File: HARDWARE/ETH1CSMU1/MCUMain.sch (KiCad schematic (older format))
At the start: 31 parts, among them J701 Conn_02x05, U701 STM32F746ZETx, U702 24LC08, X701 CRYSTAL_4PIN

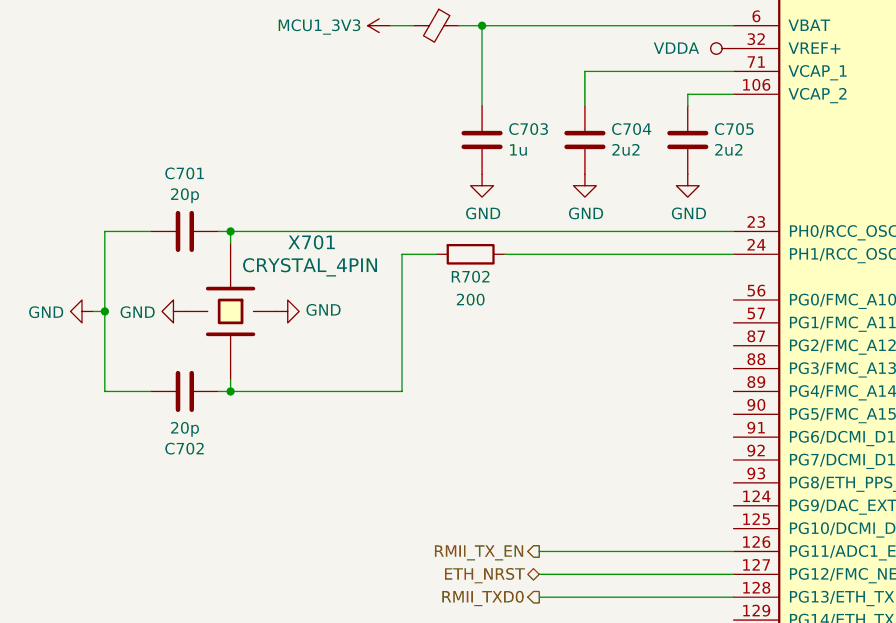
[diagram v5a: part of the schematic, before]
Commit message: Redesigned feedback circuit.
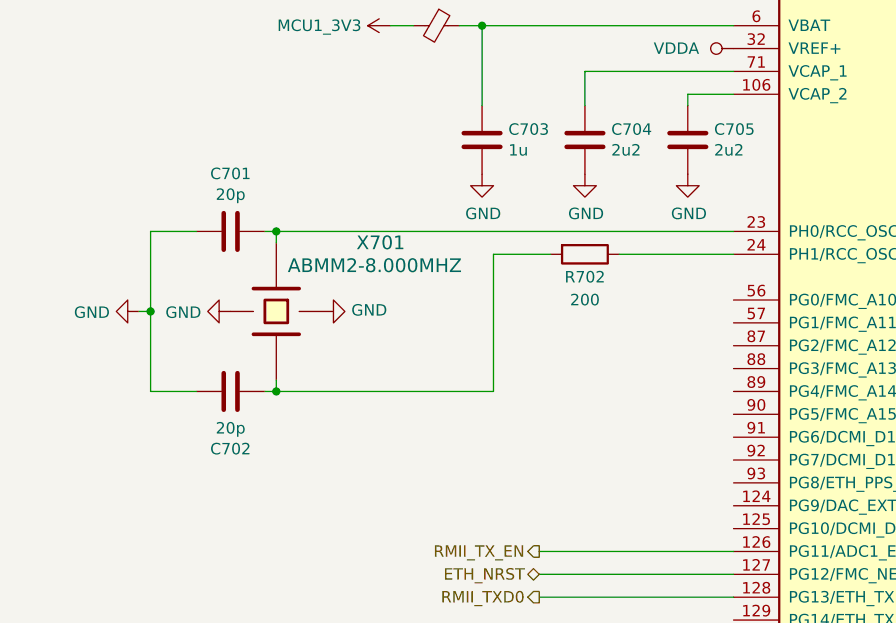
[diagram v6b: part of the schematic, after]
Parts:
- R702: footprint (none) -> Resistors_SMD:R_0603
- X701: value CRYSTAL_4PIN -> ABMM2-8.000MHZ
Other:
- moved on the sheet: C701, C702, R702, X701
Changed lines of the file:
@@
 L crystal_local:CRYSTAL_4PIN X?
 U 1 1 5BE349FE
-P 1450 3950
+P 1650 3950
 AR Path="/5BE0F4FE/5BE349FE" Ref="X?"  Part="1"
 AR Path="/5BE4235D/5BE349FE" Ref="X701"  Part="1"
-F 0 "X701" V 1150 4200 60  0000 L CNN
-F 1 "CRYSTAL_4PIN" V 1250 4000 60  0000 L CNN
-F 2 "" H 1450 3950 60  0001 C CNN
-F 3 "" H 1450 3950 60  0000 C CNN
+F 0 "X701" V 1350 4300 60  0000 L CNN
+F 1 "ABMM2-8.000MHZ" V 1450 4000 60  0000 L CNN
+F 2 "" H 1650 3950 60  0001 C CNN
+F 3 "" H 1650 3950 60  0000 C CNN
+	1    1650 3950
+	0    1    1    0
+$EndComp
+Wire Wire Line
+	1650 3650 1650 3600
+Wire Wire Line
+	1650 4250 1650 4300
+Wire Wire Line
+	1650 4300 2600 4300
+$Comp
+L Device:C C?
+U 1 1 5BE34A08
+P 1450 3600
+AR Path="/5BE0F4FE/5BE34A08" Ref="C?"  Part="1"
+AR Path="/5BE4235D/5BE34A08" Ref="C701"  Part="1"
+F 0 "C701" V 1198 3600 50  0000 C CNN
+F 1 "20p" V 1289 3600 50  0000 C CNN
+F 2 "Capacitors_SMD:C_0603" H 1488 3450 50  0001 C CNN
+F 3 "~" H 1450 3600 50  0001 C CNN
+	1    1450 3600
+	0    1    1    0
+$EndComp
+Wire Wire Line
+	1600 3600 1650 3600
+$Comp
+L Device:C C?
+U 1 1 5BE34A11
+P 1450 4300
+AR Path="/5BE0F4FE/5BE34A11" Ref="C?"  Part="1"
+AR Path="/5BE4235D/5BE34A11" Ref="C702"  Part="1"
+F 0 "C702" V 1702 4300 50  0000 C CNN
+F 1 "20p" V 1611 4300 50  0000 C CNN
+F 2 "Capacitors_SMD:C_0603" H 1488 4150 50  0001 C CNN
+F 3 "~" H 1450 4300 50  0001 C CNN
+	1    1450 4300
+	0    -1   1    0
+$EndComp
+Wire Wire Line
+	1600 4300 1650 4300
+Connection ~ 1650 4300
+Wire Wire Line
+	1300 4300 1100 4300
+Wire Wire Line
+	1100 4300 1100 3950
+Wire Wire Line
+	1100 3600 1300 3600
+Wire Wire Line
+	1050 3950 1100 3950
+Connection ~ 1100 3950
+Wire Wire Line
+	1100 3950 1100 3600
+$Comp
+L power:GND #PWR?
+U 1 1 5BE34A20
+P 1450 3950
+AR Path="/5BE0F4FE/5BE34A20" Ref="#PWR?"  Part="1"
+AR Path="/5BE4235D/5BE34A20" Ref="#PWR0101"  Part="1"
+F 0 "#PWR0101" H 1450 3700 50  0001 C CNN
+F 1 "GND" V 1455 3822 50  0000 R CNN
+F 2 "" H 1450 3950 50  0001 C CNN
+F 3 "" H 1450 3950 50  0001 C CNN
 	1    1450 3950
 	0    1    1    0
 $EndComp
-Wire Wire Line
-	1450 3650 1450 3600
-Wire Wire Line
-	1450 4250 1450 4300
-Wire Wire Line
-	1450 4300 2200 4300
-$Comp
-L Device:C C?
-U 1 1 5BE34A08
-P 1250 3600
-AR Path="/5BE0F4FE/5BE34A08" Ref="C?"  Part="1"
-AR Path="/5BE4235D/5BE34A08" Ref="C701"  Part="1"
-F 0 "C701" V 998 3600 50  0000 C CNN
-F 1 "20p" V 1089 3600 50  0000 C CNN
-F 2 "Capacitors_SMD:C_0603" H 1288 3450 50  0001 C CNN
-F 3 "~" H 1250 3600 50  0001 C CNN
-	1    1250 3600
-	0    1    1    0
-$EndComp
-Wire Wire Line
-	1400 3600 1450 3600
-Connection ~ 1450 3600
-$Comp
-L Device:C C?
-U 1 1 5BE34A11
-P 1250 4300
-AR Path="/5BE0F4FE/5BE34A11" Ref="C?"  Part="1"
-AR Path="/5BE4235D/5BE34A11" Ref="C702"  Part="1"
-F 0 "C702" V 1502 4300 50  0000 C CNN
-F 1 "20p" V 1411 4300 50  0000 C CNN
-F 2 "Capacitors_SMD:C_0603" H 1288 4150 50  0001 C CNN
-F 3 "~" H 1250 4300 50  0001 C CNN
-	1    1250 4300
-	0    -1   1    0
-$EndComp
-Wire Wire Line
-	1400 4300 1450 4300
-Connection ~ 1450 4300
-Wire Wire Line
-	1100 4300 900  4300
-Wire Wire Line
-	900  4300 900  3950
-Wire Wire Line
-	900  3600 1100 3600
-Wire Wire Line
-	850  3950 900  3950
-Connection ~ 900  3950
-Wire Wire Line
-	900  3950 900  3600
-$Comp
-L power:GND #PWR?
-U 1 1 5BE34A20
-P 1250 3950
-AR Path="/5BE0F4FE/5BE34A20" Ref="#PWR?"  Part="1"
-AR Path="/5BE4235D/5BE34A20" Ref="#PWR0101"  Part="1"
-F 0 "#PWR0101" H 1250 3700 50  0001 C CNN
-F 1 "GND" V 1255 3822 50  0000 R CNN
-F 2 "" H 1250 3950 50  0001 C CNN
-F 3 "" H 1250 3950 50  0001 C CNN
-	1    1250 3950
-	0    1    1    0
-$EndComp
 $Comp
 L power:GND #PWR?
 U 1 1 5BE34A26
-P 1650 3950
+P 1850 3950
 AR Path="/5BE0F4FE/5BE34A26" Ref="#PWR?"  Part="1"
 AR Path="/5BE4235D/5BE34A26" Ref="#PWR0102"  Part="1"
-F 0 "#PWR0102" H 1650 3700 50  0001 C CNN
-F 1 "GND" V 1655 3822 50  0000 R CNN
-F 2 "" H 1650 3950 50  0001 C CNN
-F 3 "" H 1650 3950 50  0001 C CNN
-	1    1650 3950
+F 0 "#PWR0102" H 1850 3700 50  0001 C CNN
+F 1 "GND" V 1855 3822 50  0000 R CNN
+F 2 "" H 1850 3950 50  0001 C CNN
+F 3 "" H 1850 3950 50  0001 C CNN
+	1    1850 3950
 	0    -1   -1   0
 $EndComp
@@
 L power:GND #PWR?
 U 1 1 5BE34A2C
-P 850 3950
+P 1050 3950
 AR Path="/5BE0F4FE/5BE34A2C" Ref="#PWR?"  Part="1"
 AR Path="/5BE4235D/5BE34A2C" Ref="#PWR0103"  Part="1"
-F 0 "#PWR0103" H 850 3700 50  0001 C CNN
-F 1 "GND" V 855 3822 50  0000 R CNN
-F 2 "" H 850 3950 50  0001 C CNN
-F 3 "" H 850 3950 50  0001 C CNN
-	1    850  3950
+F 0 "#PWR0103" H 1050 3700 50  0001 C CNN
+F 1 "GND" V 1055 3822 50  0000 R CNN
+F 2 "" H 1050 3950 50  0001 C CNN
+F 3 "" H 1050 3950 50  0001 C CNN
+	1    1050 3950
 	0    1    1    0
 $EndComp
 Wire Wire Line
-	2200 3700 2200 4300
-Wire Wire Line
-	2350 3700 2200 3700
+	2600 3700 2600 4300
 $Comp
 L Device:R R702
 U 1 1 5BE36AF2
-P 2500 3700
-F 0 "R702" V 2600 3700 50  0000 C CNN
-F 1 "200" V 2700 3700 50  0000 C CNN
-F 2 "" V 2430 3700 50  0001 C CNN
-F 3 "~" H 2500 3700 50  0001 C CNN
-	1    2500 3700
+P 3000 3700
+F 0 "R702" V 3100 3700 50  0000 C CNN
+F 1 "200" V 3200 3700 50  0000 C CNN
+F 2 "Resistors_SMD:R_0603" V 2930 3700 50  0001 C CNN
+F 3 "~" H 3000 3700 50  0001 C CNN
+	1    3000 3700
 	0    1    1    0
 $EndComp
@@
 $EndComp
 Wire Wire Line
-	2650 3700 3650 3700
-Wire Wire Line
-	1450 3600 3650 3600
+	3150 3700 3650 3700
 $Comp
 L power:VDDA #PWR0708
@@
 	0    1    1    0
 $EndComp
+Wire Wire Line
+	3650 3600 1650 3600
+Connection ~ 1650 3600
+Wire Wire Line
+	2600 3700 2850 3700
 $EndSCHEMATC

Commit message: Schematic development
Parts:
- renumbered C720 to C601, C701 to C602, C702 to C603, C706 to C604, C707 to C605, C703 to C606, C704 to C607, C708 to C608, C705 to C609, C709 to C610, C710 to C611, C711 to C612, C712 to C613, C713 to C614, C714 to C615, C715 to C616, C716 to C617, C717 to C618, C718 to C619, C719 to C620, FB702 to FB601, FB701 to FB602, J701 to J601, R703 to R601, R702 to R602, R701 to R603, R704 to R604, R705 to R605, U701 to U601, U702 to U602, X701 to X601
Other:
- moved on the sheet: C604, C605, C608, C610, C611, C612, C613, C614, C615, C616, C617, C618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
